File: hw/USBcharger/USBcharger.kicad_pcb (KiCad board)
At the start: 2 copper layers, 31 x 18 mm, 33 parts, among them J1 Conn_01x03, J2 Conn_01x03, J3 Conn_01x01, J4 Conn_01x01, J5 Conn_01x01, J6 Conn_01x01, U1 LTC2309_QFN

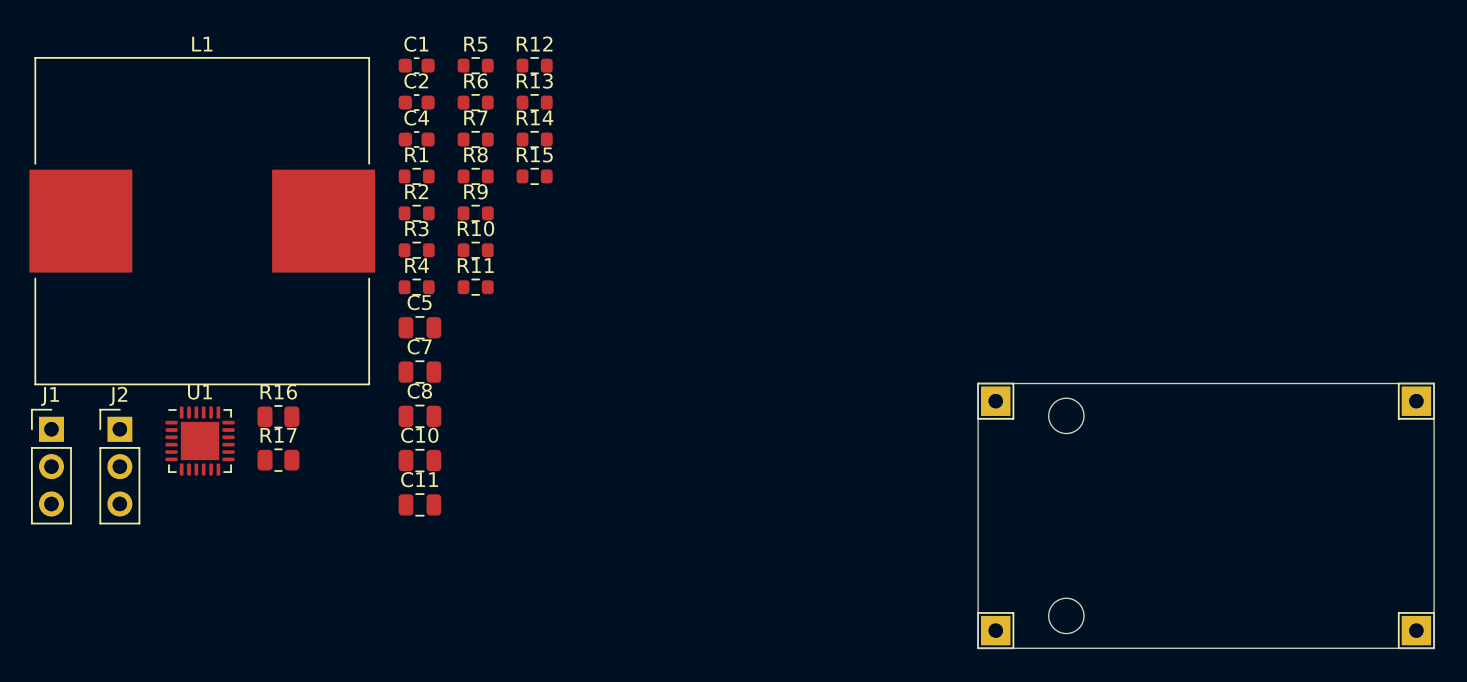
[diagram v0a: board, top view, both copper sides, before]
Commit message: created model of the chinese charger module
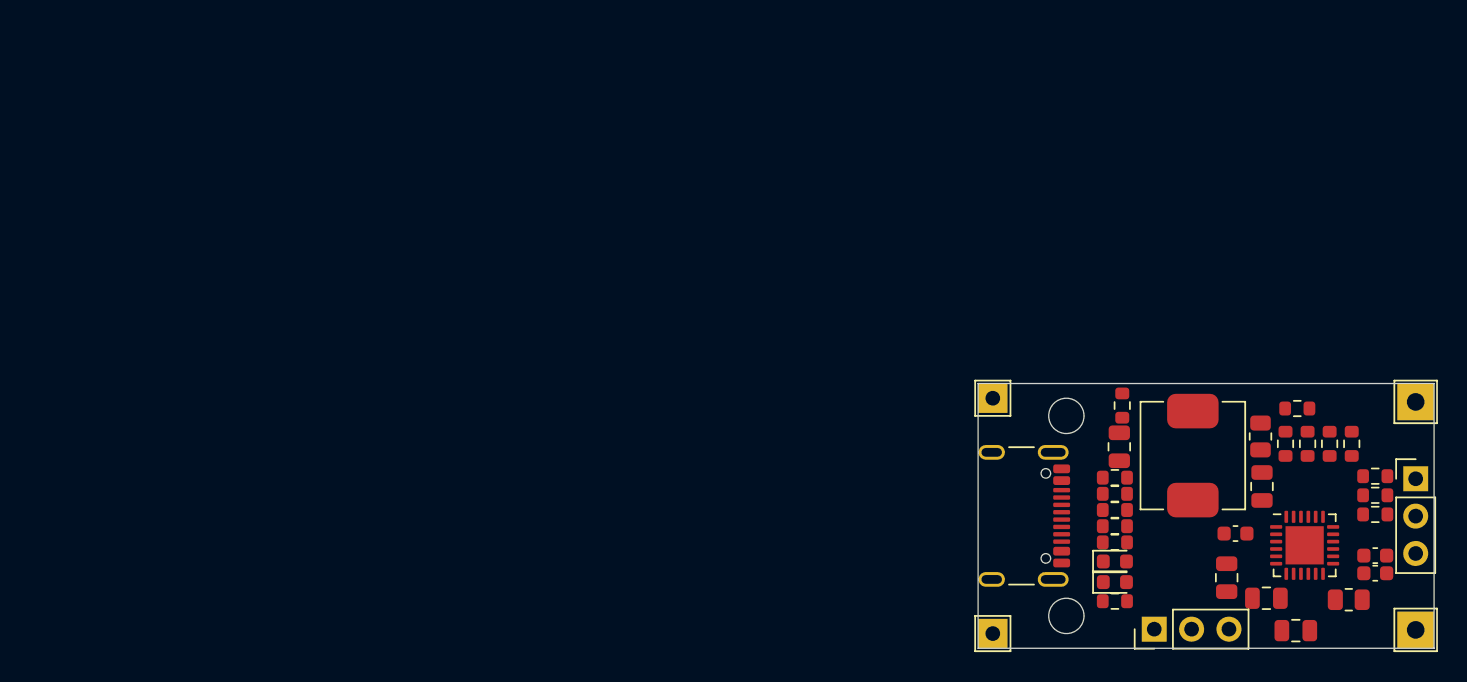
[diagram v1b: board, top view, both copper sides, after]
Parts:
- added D1: LED, LED_SMD:LED_0603_1608Metric, F.Cu at (149.3, 83.5)
- added D2: LED, LED_SMD:LED_0603_1608Metric, F.Cu at (149.3, 82.1)
- added P1: USB_C_Plug, Connector_USB:USB_C_Receptacle_GCT_USB4105-xx-A_16P_TopMnt_Horizontal, F.Cu at (142.0, 79.0)
- J5, J6: footprint TestPoint:TestPoint_THTPad_2.0x2.0mm_Drill1.0mm -> TestPoint:TestPoint_THTPad_2.5x2.5mm_Drill1.2mm
- L1: footprint Inductor_SMD:L_Wuerth_HCI-2212 -> Inductor_SMD:L_APV_APH0620
- moved J2 88.2 mm to (169.8, 76.5)
- moved J1 76.2 mm to (152.0, 86.7), turned to 90 degrees
- moved U1 75.4 mm to (162.2, 81.0)
- moved R17 73.4 mm to (165.2, 84.7)
- moved C1 73.2 mm to (167.0, 81.7)
- moved C2 72.6 mm to (167.0, 82.9)
- moved L1 69.2 mm to (154.6, 74.9), turned to 90 degrees
- moved R1 68.7 mm to (167.0, 77.6)
- moved R3 67.6 mm to (167.0, 78.9)
- moved R2 67.6 mm to (167.0, 76.3)
- moved R16 66.8 mm to (159.2, 73.6), turned to 90 degrees
- moved C4 61.8 mm to (157.5, 80.2)
- moved R9 61.6 mm to (165.4, 74.1), turned to 90 degrees
- moved R8 60.8 mm to (163.9, 74.1), turned to 90 degrees
- moved R5 60.5 mm to (161.7, 71.7)
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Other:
- copper layers 2 -> 11
